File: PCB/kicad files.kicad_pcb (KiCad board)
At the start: 2 copper layers, 3.6 x 3.3 mm, 35 parts, among them J2 Conn_01x04_Pin, SW1 SW_Push_45deg, SW10 RotaryEncoder_Switch, SW2 SW_Push_45deg, SW3 SW_Push_45deg, SW4 SW_Push_45deg, SW5 SW_Push_45deg, SW6 SW_Push_45deg, SW7 SW_Push_45deg, SW8 SW_Push_45deg, SW9 SW_Push_45deg, U2 MOUDLE-SEEEDUINO-XIAO

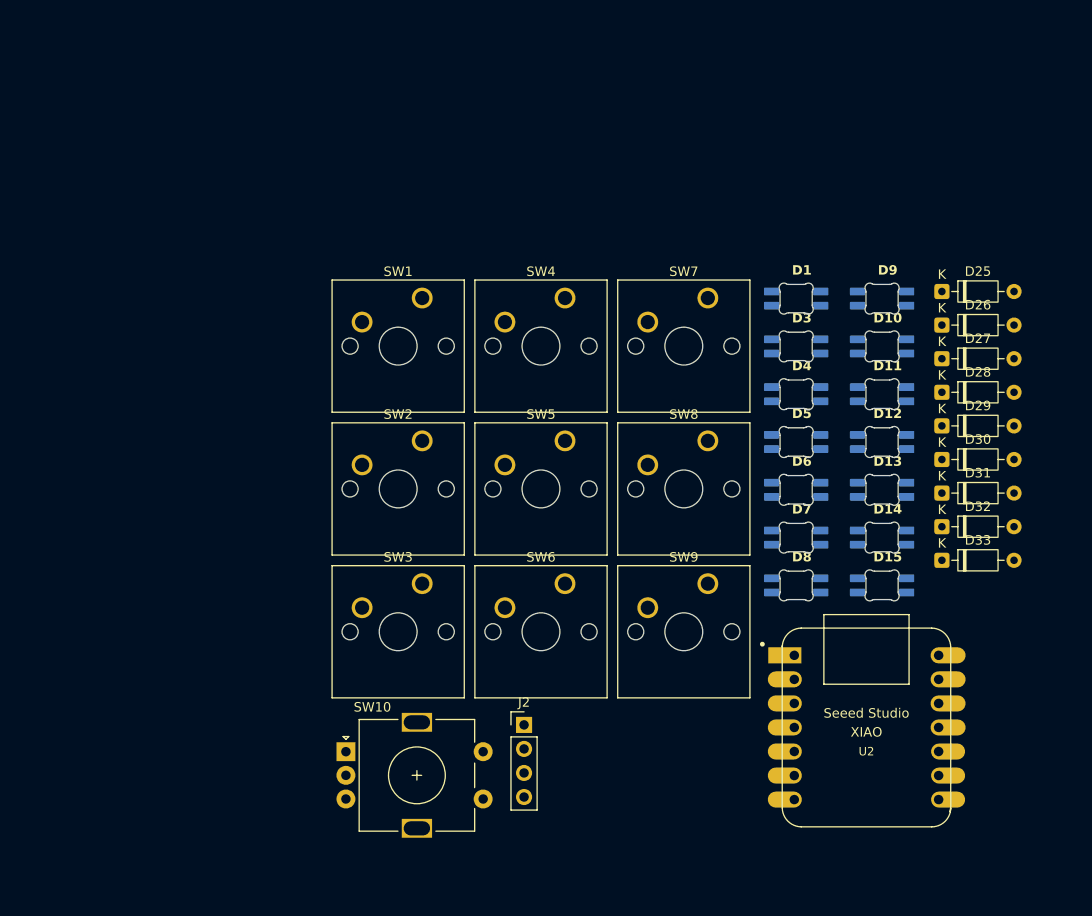
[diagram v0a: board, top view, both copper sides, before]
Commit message: diode placement
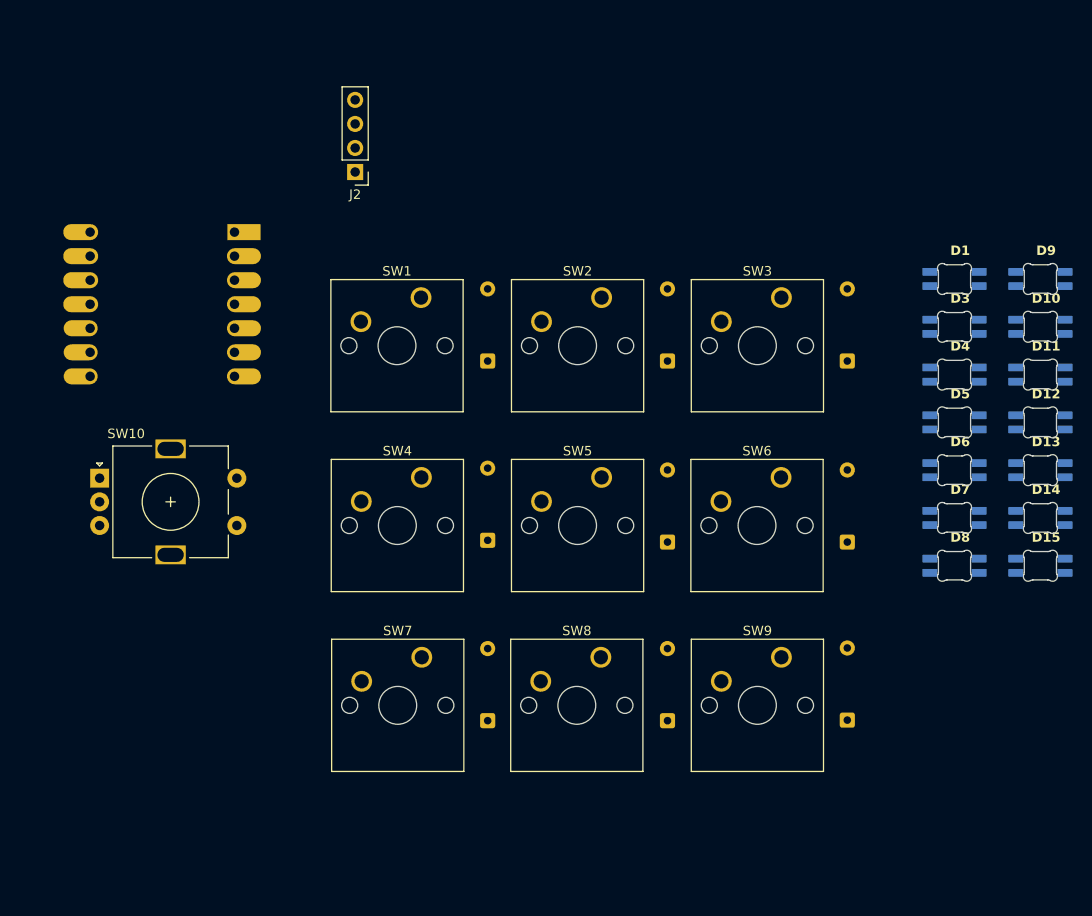
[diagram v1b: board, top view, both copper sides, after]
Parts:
- D25, D26, D27, D28, D29, D30, D31, D32, D33, U2: moved to B.Cu
- moved U2 86.8 mm to (94.1, 71.1), turned to 180 degrees
- moved J2 61.1 mm to (114.5, 57.1), turned to 180 degrees
- moved D31 53.7 mm to (128.5, 115.1), turned to 90 degrees
- moved D28 50.5 mm to (128.5, 96.1), turned to 90 degrees
- moved D25 48.6 mm to (128.5, 77.1), turned to 90 degrees
- moved SW3 48.5 mm to (159.5, 70.4)
- moved SW7 48.5 mm to (121.5, 108.4)
- moved SW10 38.9 mm to (87.5, 89.5)
- moved D32 35.5 mm to (147.5, 115.1), turned to 90 degrees
- moved D29 31.5 mm to (147.5, 96.2), turned to 90 degrees
- moved D26 29.2 mm to (147.5, 77.1), turned to 90 degrees
- moved SW8 25.5 mm to (140.5, 108.4)
- moved SW6 25.4 mm to (159.5, 89.4)
- moved SW4 24.3 mm to (121.5, 89.4)
- moved SW2 24.3 mm to (140.5, 70.4)
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
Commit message: placed LEDs
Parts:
- moved D10 81.1 mm to (119.0, 123.0)
- moved D14 77.7 mm to (109.5, 75.5), turned to 90 degrees
- moved D13 69.9 mm to (109.5, 113.5), turned to 90 degrees
- moved D4 68.5 mm to (119.0, 85.0)
- moved D7 62.2 mm to (119.0, 104.0)
- moved D2 58.9 mm to (138.0, 66.0)
- moved D1 58.9 mm to (119.0, 66.0)
- moved D12 57.7 mm to (157.0, 123.0)
- moved D8 52.9 mm to (138.0, 104.0)
- moved D11 49.4 mm to (138.0, 123.0)
- moved J2 42.4 mm to (156.0, 48.4), turned to 0 degrees
- moved D5 40.3 mm to (138.0, 85.0)
- moved D6 30.1 mm to (157.0, 85.0)
- moved D9 25.8 mm to (157.0, 104.0)
- moved U2 22.7 mm to (105.5, 51.5)
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- renumbered D11 to D10, D7 to D11, D10 to D12, D8 to D13, D9 to D14, D15 to D2, D14 to D4, D4 to D5, D13 to D6, D5 to D7, D12 to D8, D6 to D9
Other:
- board size 3.6 x 3.3 mm -> 93 x 90.5 mm

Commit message: pcb finally done with 64 fucking errorss
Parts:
- moved D6 70.0 mm to (98.5, 123.5)
- moved SW10 64.0 mm to (152.5, 75.0)
- moved D33 58.6 mm to (107.9, 116.5)
- moved D27 58.6 mm to (107.9, 78.5)
- moved D30 58.6 mm to (107.9, 97.5)
- moved D11 54.5 mm to (98.5, 85.5)
- moved U2 51.4 mm to (156.9, 51.5)
- moved D2 50.5 mm to (88.5, 76.0), turned to 90 degrees
- moved D9 43.6 mm to (117.5, 85.5)
- moved D4 42.2 mm to (88.5, 114.1), turned to 90 degrees
- moved D3 39.5 mm to (117.5, 66.2)
- moved D14 30.1 mm to (117.5, 104.5), turned to 0 degrees
- moved D8 28.3 mm to (117.5, 123.5)
- moved D12 27.6 mm to (136.5, 104.5)
- moved D7 25.5 mm to (136.2, 85.2)
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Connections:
- U2 pad 10: Column 1 -> column 1
- U2 pad 11: Column 0 -> column 0
- U2 pad 9: Column 2 -> column 2
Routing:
- net GND: track 0.00 -> 397.5 mm, vias 0 -> 17
- net +5V: track 0.00 -> 340.4 mm, vias 0 -> 24
- net Row 2: track 0.00 -> 114.0 mm
- net column 0: track 0.00 -> 105.3 mm
- net Row 1: track 0.00 -> 102.6 mm
- net Row 0: track 0.00 -> 86.1 mm
- net LED Data: track 0.00 -> 84.7 mm, vias 0 -> 2
- net column 1: track 0.00 -> 84.1 mm
- net ENC_A: track 0.00 -> 80.7 mm
- net ENC_B: track 0.00 -> 68.9 mm
- net column 2: track 0.00 -> 59.4 mm
- net Net-(D2-DIN): track 0.00 -> 55.1 mm, vias 0 -> 2
- net Net-(D10-DIN): track 0.00 -> 48.2 mm
- net Net-(D5-DOUT): track 0.00 -> 47.8 mm
- net SCL: track 0.00 -> 43.8 mm, vias 0 -> 2
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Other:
- board size 93 x 90.5 mm -> 96 x 92.8 mm
